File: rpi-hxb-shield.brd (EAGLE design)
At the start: 33.5 x 35 mm, 23 parts, among them Q1 CRYSTALX22, U2 24LC128-I/SN

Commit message: maximum outline, removed wire antenna
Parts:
- removed PAD1, PAD2: (no value), wirepad:SMD1,27-2,54
- moved U$1 33.5 mm to (0.50, 36.5)
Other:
- board size 33.5 x 35 mm -> 54 x 55 mm
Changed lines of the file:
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@@
 <layers>
 <layer number="1" name="Top" color="4" fill="1" visible="yes" active="yes"/>
-<layer number="16" name="Bottom" color="1" fill="1" visible="no" active="yes"/>
+<layer number="16" name="Bottom" color="1" fill="1" visible="yes" active="yes"/>
 <layer number="17" name="Pads" color="2" fill="1" visible="yes" active="yes"/>
 <layer number="18" name="Vias" color="2" fill="1" visible="yes" active="yes"/>
@@
 <wire x1="0" y1="0" x2="33.5" y2="0" width="0" layer="20"/>
 <wire x1="33.5" y1="0" x2="33.5" y2="35" width="0" layer="20"/>
-<wire x1="33.5" y1="35" x2="0" y2="35" width="0" layer="20"/>
+<wire x1="33.5" y1="35" x2="14" y2="35" width="0" layer="20"/>
+<wire x1="14" y1="35" x2="0" y2="35" width="0" layer="20"/>
 <wire x1="0" y1="35" x2="0" y2="0" width="0" layer="20"/>
-<text x="31.9" y="33" size="1.27" layer="21" font="vector" ratio="15" rot="SR270">h e x a b u s</text>
-<text x="17.4" y="24" size="1.27" layer="1" font="vector" ratio="12" rot="SR270">Fraunhofer ITWM</text>
-<text x="31.1" y="33" size="0.6096" layer="21" font="vector" distance="100" rot="SR270">the kraken of home automation</text>
-<text x="22" y="4.5" size="0.8128" layer="21" font="vector" ratio="12">hexabus</text>
-<text x="22" y="3.5" size="0.8128" layer="21" font="vector">rpi-shield</text>
-<text x="22" y="2.5" size="0.6096" layer="21" font="vector">20140206</text>
-<wire x1="14" y1="32.6" x2="30.5" y2="32.6" width="0.254" layer="48"/>
-<wire x1="30.5" y1="32.6" x2="30.5" y2="1.6" width="0.254" layer="48"/>
-<wire x1="30.5" y1="1.6" x2="21" y2="1.6" width="0.254" layer="48"/>
-<wire x1="21" y1="1.6" x2="21" y2="29.6" width="0.254" layer="48"/>
+<text x="12.3" y="52.8" size="1.27" layer="21" font="vector" ratio="15" rot="SR270">h e x a b u s</text>
+<text x="0.6" y="53.8" size="1.27" layer="1" font="vector" ratio="12" rot="SR270">Fraunhofer ITWM</text>
+<text x="10.2" y="51.8" size="0.6096" layer="21" font="vector" distance="100" rot="SR270">the kraken of home automation</text>
+<text x="3.2" y="54.5" size="0.8128" layer="21" font="vector" ratio="12">hexabus</text>
+<text x="2.8" y="53.4" size="0.8128" layer="21" font="vector">rpi-shield</text>
+<text x="3" y="35.6" size="0.6096" layer="21" font="vector">20140206</text>
 <dimension x1="0" y1="0" x2="33.5" y2="0" x3="16.75" y3="-2.6" textsize="1.778" layer="48"/>
 <dimension x1="0" y1="0" x2="0" y2="35" x3="-2.6" y3="17.5" textsize="1.778" layer="48"/>
@@
 <text x="16.6" y="3" size="0.8128" layer="16" font="vector" rot="MR0">rpi-shield</text>
 <text x="16.6" y="1.5" size="0.6096" layer="16" font="vector" rot="MR0">20140206</text>
+<wire x1="14" y1="35" x2="14" y2="55" width="0" layer="20"/>
+<wire x1="14" y1="55" x2="54" y2="55" width="0" layer="20"/>
+<wire x1="54" y1="55" x2="54" y2="0" width="0" layer="20"/>
+<wire x1="54" y1="0" x2="33.5" y2="0" width="0" layer="20"/>
 </plain>
 <attributes>
@@
 <attribute name="NAME" x="16.765" y="19.065" size="0.6096" layer="25" rot="R90"/>
 </element>
-<element name="PAD1" library="wirepad" package="SMD1,27-2,54" value="" x="21" y="26.8" smashed="yes" rot="R180">
-<attribute name="VALUE" x="21" y="26.8" size="0.0254" layer="27" rot="R180"/>
-</element>
-<element name="PAD2" library="wirepad" package="SMD1,27-2,54" value="" x="30.5" y="5.6" smashed="yes">
-<attribute name="VALUE" x="30.5" y="5.6" size="0.0254" layer="27"/>
-</element>
-<element name="U$1" library="artwork" package="HEXAKRAKE" value="HEXAKRAKE" x="22" y="10.8"/>
+<element name="U$1" library="artwork" package="HEXAKRAKE" value="HEXAKRAKE" x="0.5" y="36.5"/>
 <element name="U2" library="hexabus" package="SOIC127P600X175-8N" value="24LC128-I/SN" x="14.5" y="4" smashed="yes" rot="R90">
 <attribute name="PACKAGE" value="SOIC-8" x="14.5" y="4" size="1.778" layer="27" rot="R90" display="off"/>

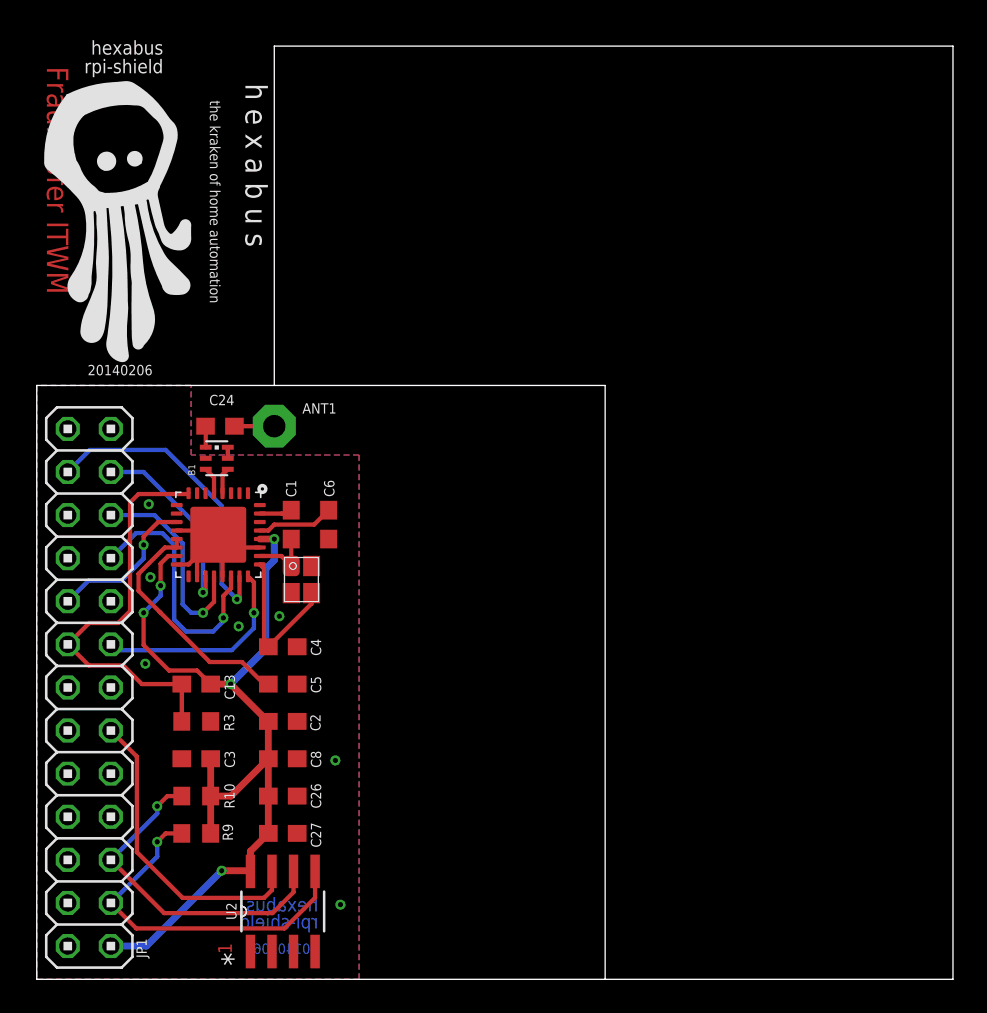
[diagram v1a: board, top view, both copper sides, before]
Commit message: changed resistors and capacitors to 0402, shuffled parts around
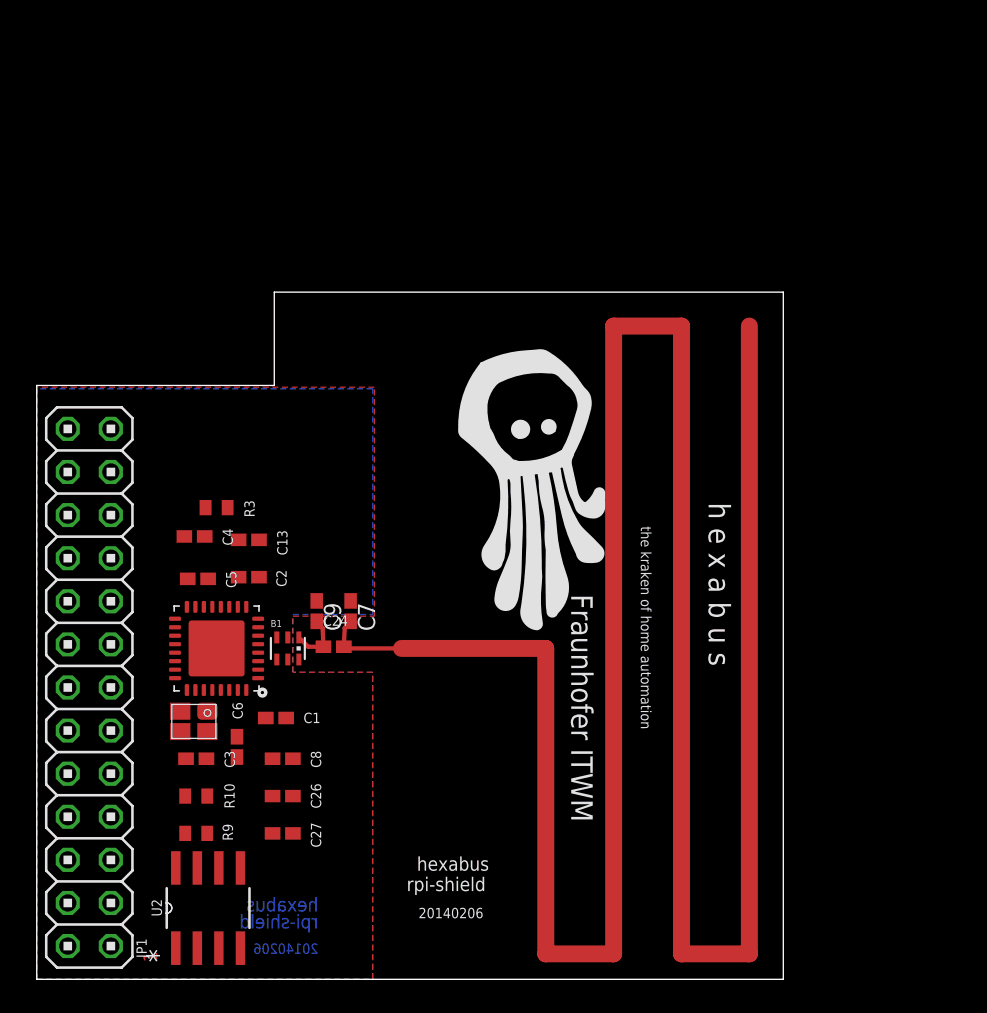
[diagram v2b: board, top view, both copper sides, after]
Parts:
- removed ANT1: (no value), discrete:PAD-01
- added C7, C9: 100pF, rcl:C0402K
- C1, C13, C2, C24, C26, C27, C3, C4, C5, C6, C8: device rcl:C0603 -> rcl:C0402K
- R10, R3, R9: device rcl:R0603 -> rcl:R0402
- moved U$1 29.1 mm to (24.9, 20.7)
- moved C24 14.6 mm to (17.5, 19.6)
- moved C6 14.2 mm to (11.8, 13.7)
- moved R3 12.7 mm to (10.6, 27.8)
- moved B1 12.0 mm to (14.8, 19.5), turned to 0 degrees
- moved C1 11.4 mm to (14.1, 15.4), turned to 0 degrees
- moved Q1 10.5 mm to (9.26, 15.2), turned to 180 degrees
- moved C13 9.05 mm to (12.5, 25.9)
- moved C2 8.73 mm to (12.5, 23.7)
- moved C4 8.32 mm to (9.30, 26.1)
- moved C5 7.96 mm to (9.50, 23.6)
- moved U1 6.70 mm to (10.6, 19.5), turned to 180 degrees
- moved U2 4.40 mm to (10.1, 4.20)
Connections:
- removed net N$34: ANT1.1, C24.2
- new net ANTENNA: C24.2, C7.2
- net GND: now also C7.1, C9.1
- net N$33: now also C9.2
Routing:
- net N$4: track 0.00 -> 149.5 mm
- net VCC: track 54.4 -> 0.00 mm, vias 5 -> 0
- net AT_RST: track 24.4 -> 0.00 mm
- net SDA: track 21.3 -> 0.00 mm, vias 1 -> 0
- net SCL: track 19.8 -> 0.00 mm, vias 1 -> 0
- net SEL1: track 18.3 -> 0.00 mm, vias 1 -> 0
- net WP: track 18.2 -> 0.00 mm
- net MOSI: track 15.3 -> 0.00 mm, vias 1 -> 0
- net N$2: track 14.3 -> 0.00 mm
- net GND: track 14.3 -> 0.00 mm, vias 7 -> 0
- net MISO: track 12.3 -> 0.00 mm, vias 1 -> 0
- net IRQ: track 12.3 -> 0.00 mm, vias 1 -> 0
- net SCLK: track 11.5 -> 0.00 mm, vias 1 -> 0
- net N$31: track 9.47 -> 0.00 mm
- net SLP_TR: track 9.12 -> 0.00 mm, vias 1 -> 0
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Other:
- board size 54 x 55 mm -> 44 x 40.5 mm

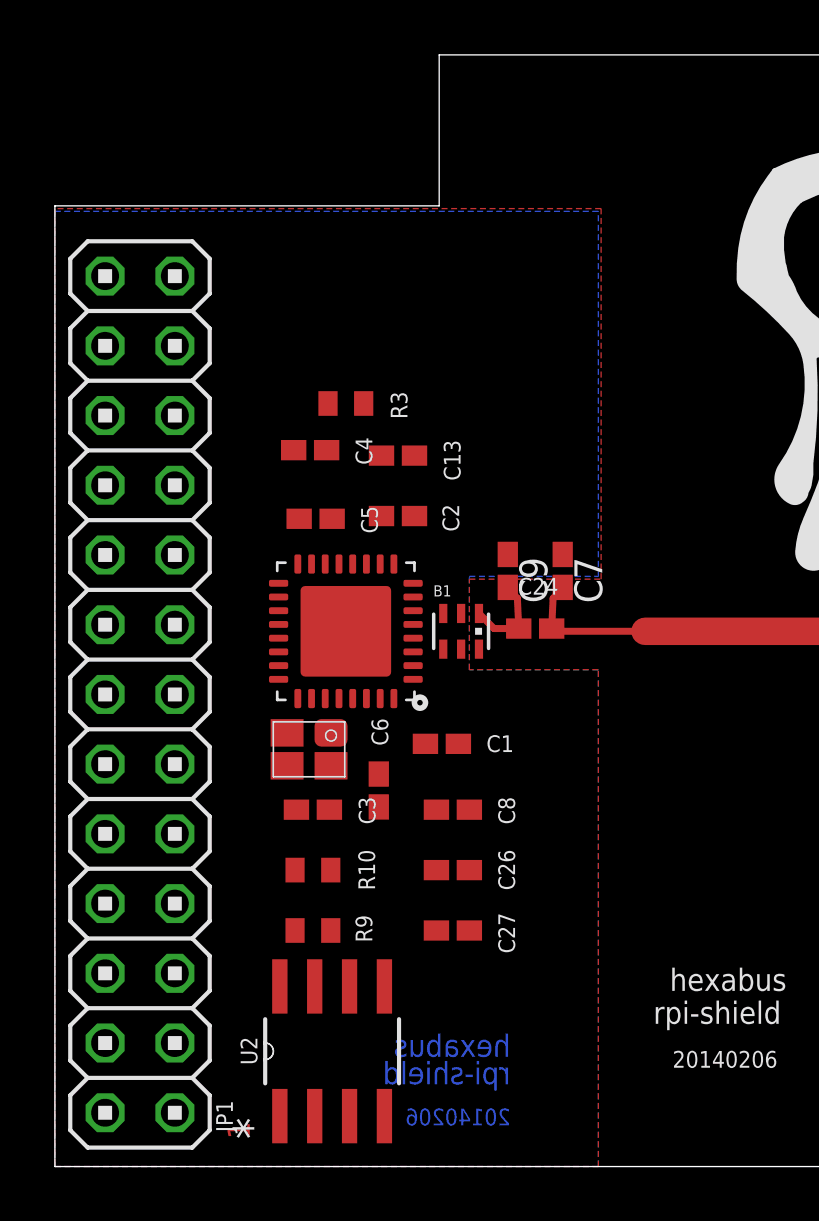
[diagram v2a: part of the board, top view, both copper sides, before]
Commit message: arranged parts in sort of a grid
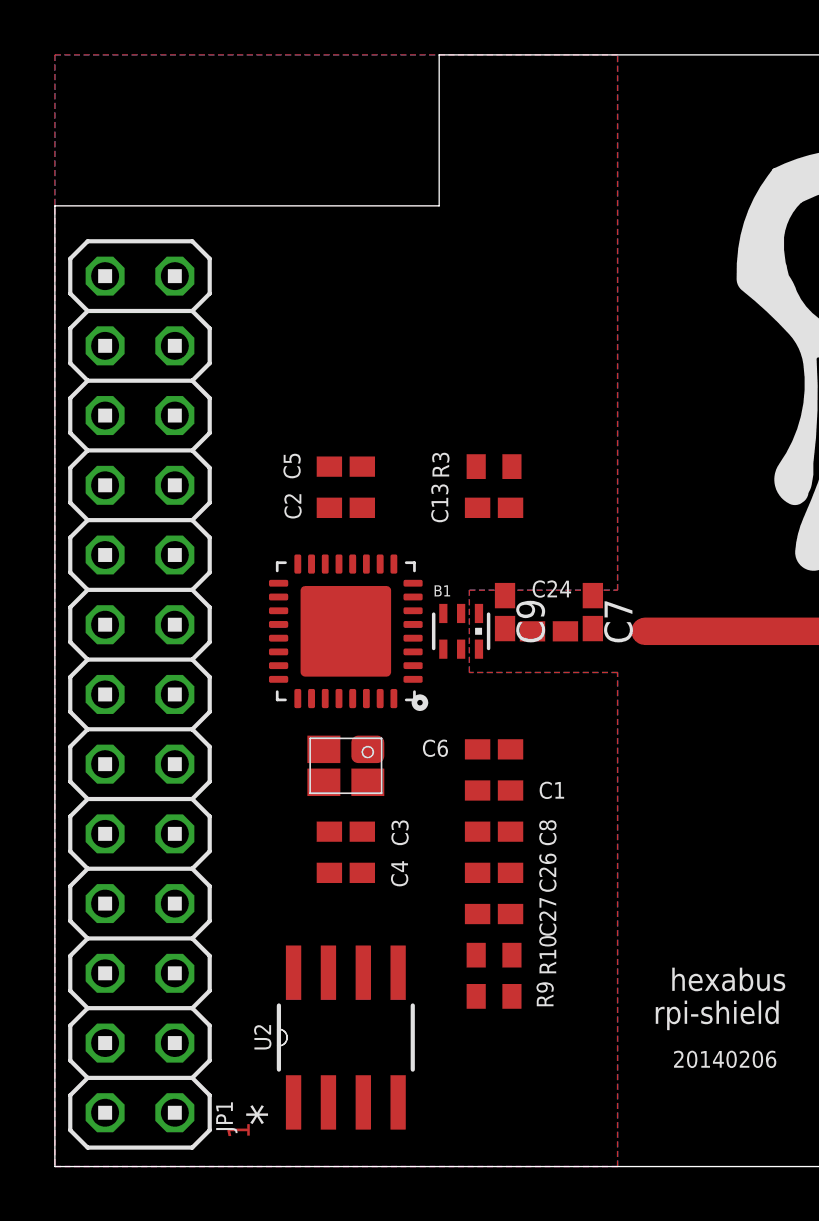
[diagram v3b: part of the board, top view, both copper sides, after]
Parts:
- moved C4 15.5 mm to (10.6, 10.7)
- moved R10 7.29 mm to (16.0, 7.70)
- moved R9 7.02 mm to (16.0, 6.20)
- moved R3 5.87 mm to (16.0, 25.5), turned to 0 degrees
- moved C6 4.46 mm to (16.0, 15.2), turned to 0 degrees
- moved C13 3.98 mm to (16.0, 24.0), turned to 0 degrees
- moved C1 2.55 mm to (16.0, 13.7)
- moved C5 2.20 mm to (10.6, 25.5), turned to 180 degrees
- moved C2 1.92 mm to (10.6, 24.0), turned to 180 degrees
- moved C7 1.86 mm to (19.6, 20.2)
- moved C8 1.70 mm to (16.0, 12.2)
- moved C27 1.62 mm to (16.0, 9.20)
- moved C26 1.50 mm to (16.0, 10.7)
- moved C9 1.50 mm to (16.4, 20.2)
- moved Q1 1.47 mm to (10.6, 14.6)
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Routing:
- net N$4: track 149.5 -> 0.00 mm
- net ANTENNA: track 1.63 -> 149.5 mm
- net N$33: track 3.31 -> 0.00 mm
- net N$5: track 3.20 -> 0.00 mm

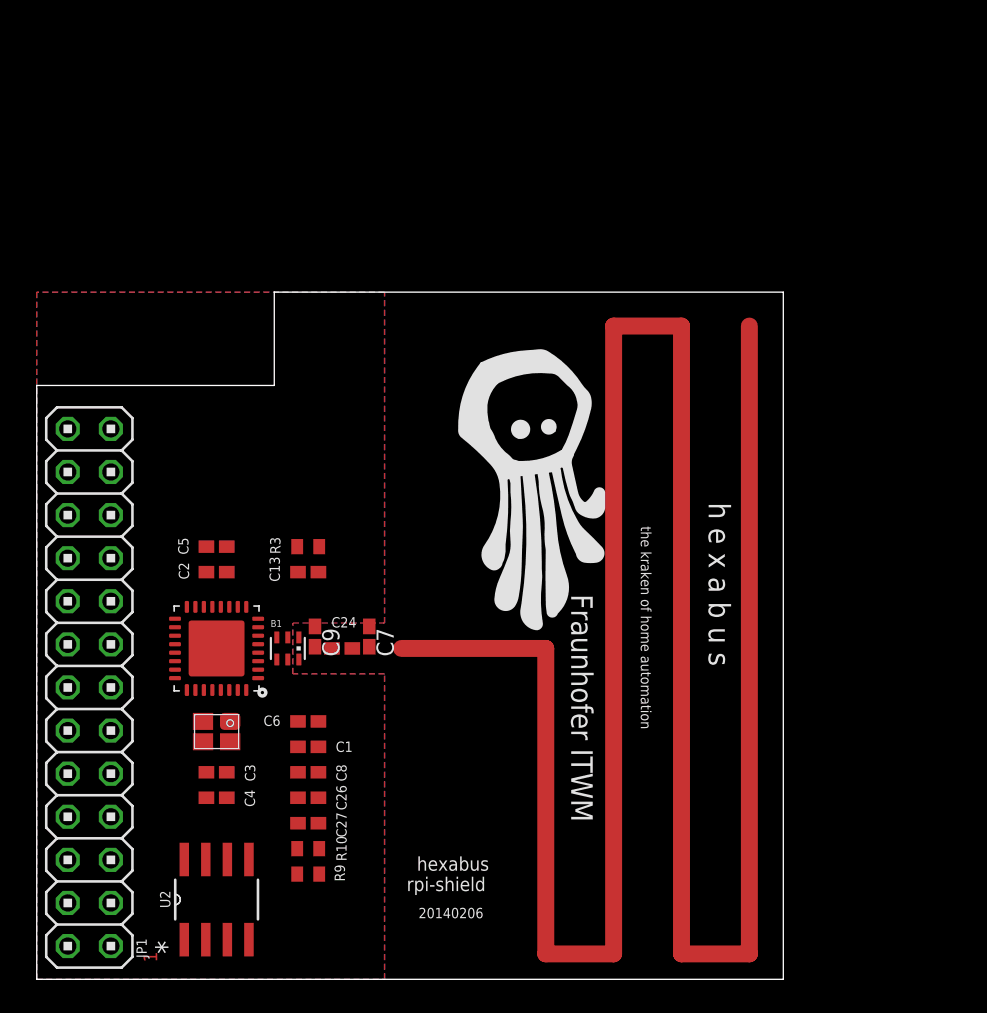
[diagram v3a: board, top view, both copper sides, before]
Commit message: vias for antenna
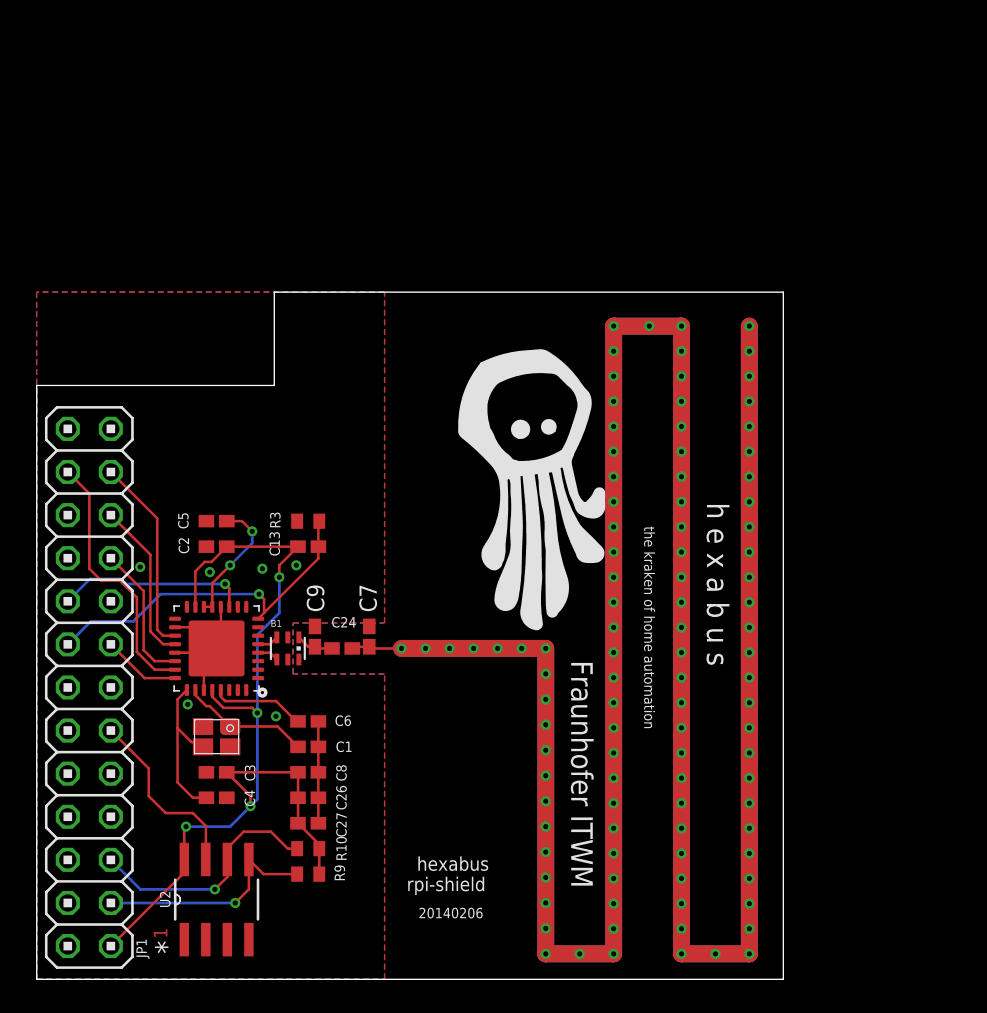
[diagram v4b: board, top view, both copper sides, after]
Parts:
- moved C13 1.50 mm to (16.0, 25.5)
- moved C2 1.50 mm to (10.6, 25.5)
- moved C5 1.50 mm to (10.6, 27.0)
- moved R3 1.50 mm to (16.0, 27.0)
- moved Q1 0.30 mm to (10.6, 14.3)
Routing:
- net ANTENNA: track 149.5 -> 302.0 mm, vias 0 -> 25
- net VCC: track 0.00 -> 55.1 mm, vias 0 -> 4
- net AT_RST: track 0.00 -> 21.0 mm, vias 0 -> 1
- net GND: track 0.00 -> 17.4 mm, vias 0 -> 6
- net SEL1: track 0.00 -> 15.6 mm
- net SCL: track 0.00 -> 14.5 mm, vias 0 -> 1
- net SDA: track 0.00 -> 13.4 mm, vias 0 -> 1
- net SCLK: track 0.00 -> 11.6 mm
- net SLP_TR: track 0.00 -> 11.4 mm, vias 0 -> 1
- net WP: track 0.00 -> 10.9 mm
- net N$31: track 0.00 -> 9.64 mm
- net MISO: track 0.00 -> 9.59 mm
- net MOSI: track 0.00 -> 8.34 mm
- net N$30: track 0.00 -> 8.01 mm
- net N$2: track 0.00 -> 7.67 mm, vias 0 -> 2
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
